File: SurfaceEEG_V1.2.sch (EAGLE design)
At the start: 52 parts

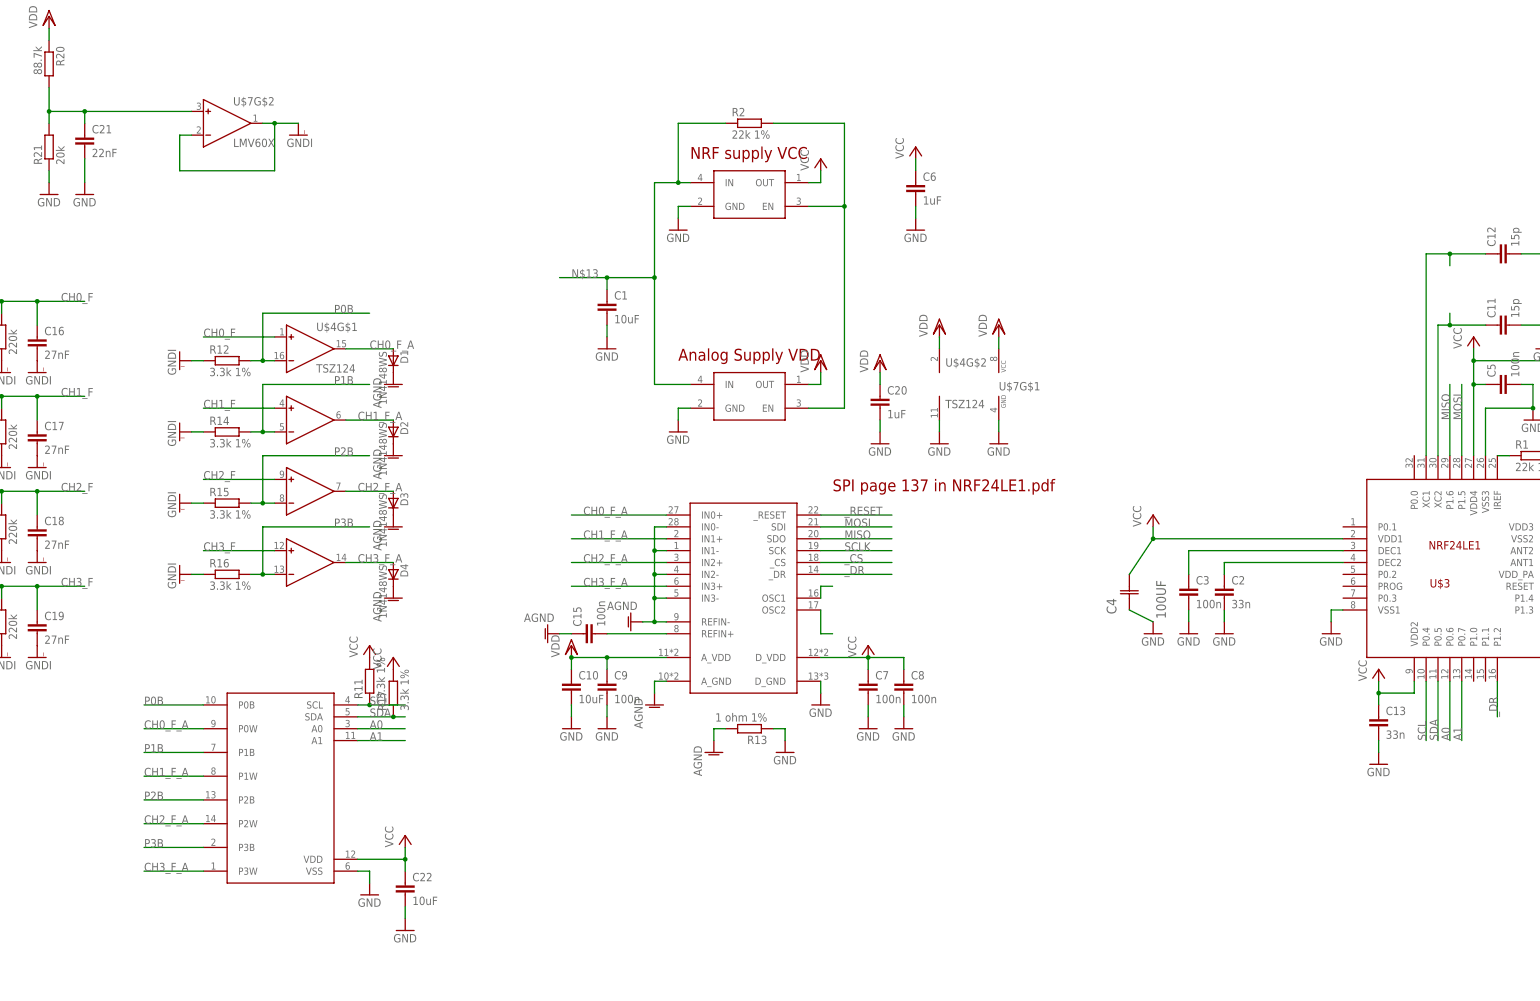
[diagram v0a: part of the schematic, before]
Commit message: Replaced components with ones from our libraries
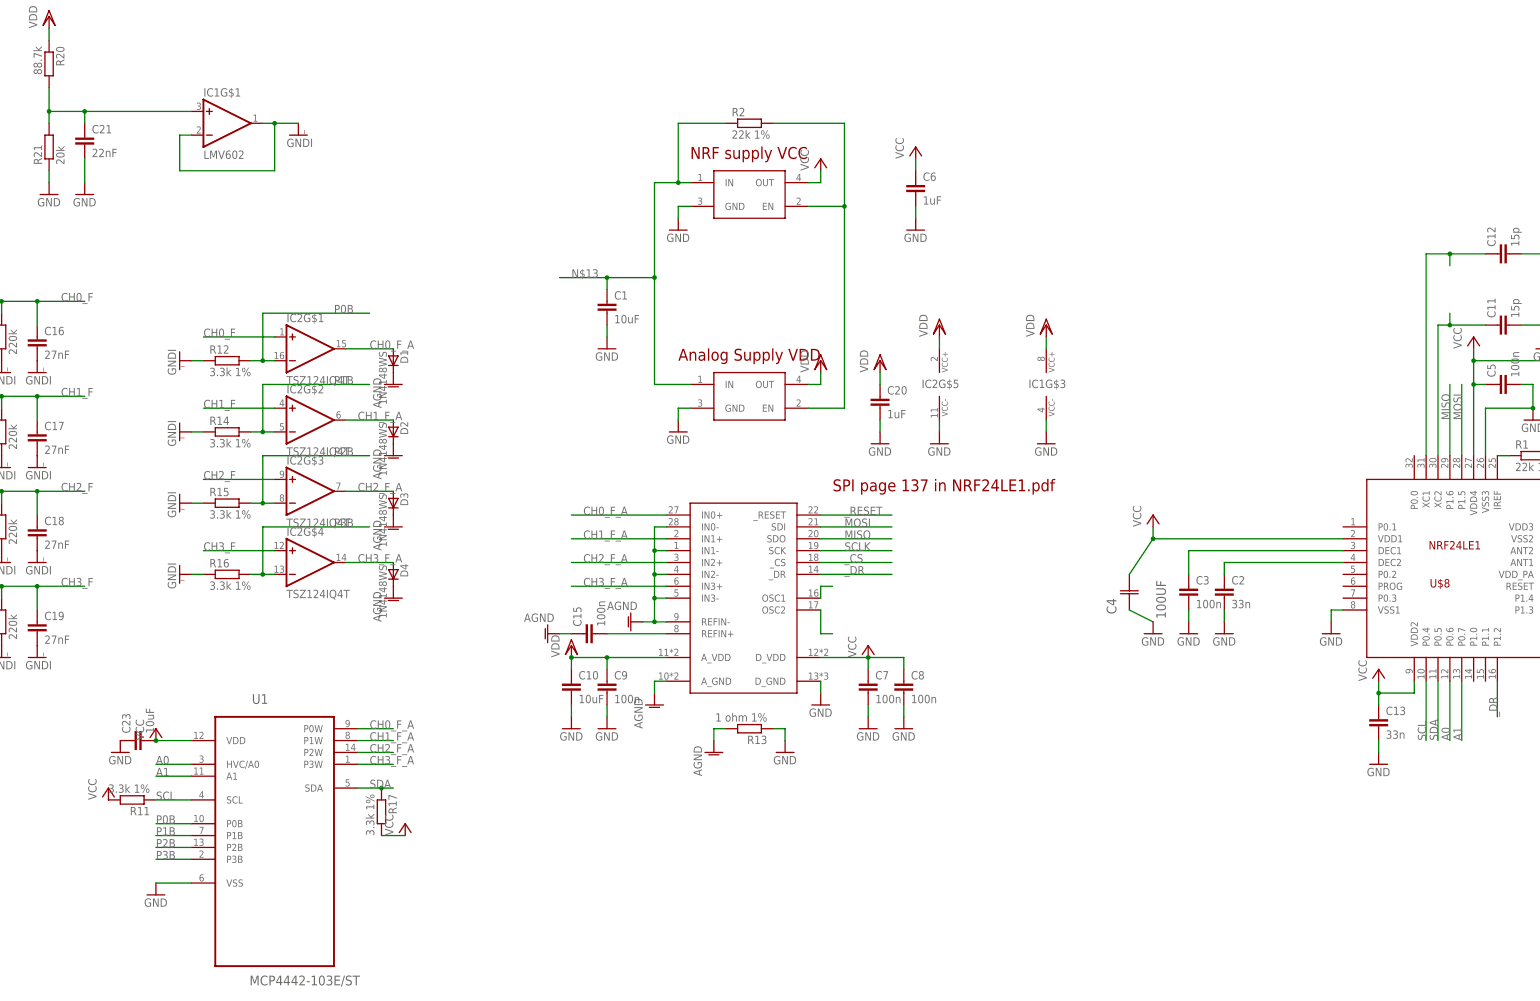
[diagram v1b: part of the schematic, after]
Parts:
- removed C22: 10uF, ELL-i-Passives:C0603
- removed U$4: TSZ124, st-microelectronics:TSZ124
- removed U$5: NCP103, on-semiconductor:NCP103
- removed U$6: MCP444X, microchip:MCP444X
- removed U$7: LMV60X, texas:LMV60X
- added C23: 10uF, ELL-i-Passives:C0603
- added IC1: LMV602, (custom)-new-components:LMV602
- added IC2: TSZ124IQ4T, (user-cadsoft)-st-microelectronics-tsz12x:TSZ124IQ4T
- added U$8: NRF24LE1, (misc)-parts-that-we-use:NRF24LE1
- added U1: MCP4442-103E/ST, (manufact)-Microchip-MCP44-farnell:MCP4442-103E/ST
- U$1: value MCP3912 -> NCP103; device microchip:MCP3912 -> (custom)-new-components:NCP103
- U$2: device on-semiconductor:NCP103 -> (custom)-new-components:NCP103
- U$3: value NRF24LE1 -> MCP3912; device SparkFun-RF:NRF24LE1 -> (custom)-new-components:MCP3912
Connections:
- net A0: now also U$8.P0.6, U1.HVC/A0; no longer U$3.P0.6, U$6.A0
- net A1: now also U$8.P0.7, U1.A1; no longer U$3.P0.7, U$6.A1
- net AGND: now also U$3.A_GND, U$3.IN0-, U$3.IN1-, U$3.IN2-, U$3.IN3-, U$3.REFIN-; no longer U$1.A_GND, U$1.IN0-, U$1.IN1-, U$1.IN2-, U$1.IN3-, U$1.REFIN-
- net CH0_F: now also IC2G$1.IN+; no longer U$4G$1.IN+
- net CH0_F_A: now also IC2G$1.OUT, U$3.IN0+, U1.P0W; no longer U$1.IN0+, U$4G$1.OUT, U$6.P0W
- net CH1_F: now also IC2G$2.IN+; no longer U$4G$1.IN+1
- net CH1_F_A: now also IC2G$2.OUT, U$3.IN1+, U1.P1W; no longer U$1.IN1+, U$4G$1.OUT1, U$6.P1W
- net CH2_F: now also IC2G$3.IN+; no longer U$4G$1.IN+2
- net CH2_F_A: now also IC2G$3.OUT, U$3.IN2+, U1.P2W; no longer U$1.IN2+, U$4G$1.OUT2, U$6.P2W
- net CH3_F: now also IC2G$4.IN+; no longer U$4G$1.IN+3
- net CH3_F_A: now also IC2G$4.OUT, U$3.IN3+, U1.P3W; no longer U$1.IN3+, U$4G$1.OUT3, U$6.P3W
- net GND: now also C23.1, IC1G$3.VCC-, IC2G$5.VCC-, U$1.GND, U$3.D_GND, U$8.VSS1, U$8.VSS2, U$8.VSS3, U1.VSS; no longer C22.2, U$1.D_GND, U$3.VSS1, U$3.VSS2, U$3.VSS3, U$4G$2.V-, U$5.GND, U$6.VSS, U$7G$1.GND
- net GNDI: now also IC1G$1.IN-, IC1G$1.OUT; no longer U$7G$2.IN-, U$7G$2.OUT
- net MISO: now also U$3.SDO, U$8.P1.6; no longer U$1.SDO, U$3.P1.6
- net MOSI: now also U$3.SDI, U$8.P1.5; no longer U$1.SDI, U$3.P1.5
- net N$10: now also U$8.XC2; no longer U$3.XC2
- net N$11: now also U$8.XC1; no longer U$3.XC1
- net N$12: now also U$3.REFIN+; no longer U$1.REFIN+
- net N$13: now also U$1.IN; no longer U$5.IN
- net N$14: now also U$3.OSC1; no longer U$1.OSC1
- net N$15: now also U$3.OSC2; no longer U$1.OSC2
- net N$18: now also IC1G$1.IN+; no longer U$7G$2.IN+
- net N$2: now also U$8.DEC1; no longer U$3.DEC1
- net N$3: now also U$8.DEC2; no longer U$3.DEC2
- net N$5: now also U$1.EN; no longer U$5.EN
- net N$6: now also U$8.ANT2; no longer U$3.ANT2
- net N$7: now also U$8.ANT1; no longer U$3.ANT1
- net N$8: now also U$8.VDD_PA; no longer U$3.VDD_PA
- net N$9: now also U$8.IREF; no longer U$3.IREF
- net P0B: now also IC2G$1.IN-, U1.P0B; no longer U$4G$1.IN-, U$6.P0B
- net P1B: now also IC2G$2.IN-, U1.P1B; no longer U$4G$1.IN-1, U$6.P1B
- net P2B: now also IC2G$3.IN-, U1.P2B; no longer U$4G$1.IN-2, U$6.P2B
- net P3B: now also IC2G$4.IN-, U1.P3B; no longer U$4G$1.IN-3, U$6.P3B
- net SCL: now also U$8.P0.4, U1.SCL; no longer U$3.P0.4, U$6.SCL
- net SCLK: now also U$3.SCK, U$8.P1.4; no longer U$1.SCK, U$3.P1.4
- net SDA: now also U$8.P0.5, U1.SDA; no longer U$3.P0.5, U$6.SDA
- net VCC: now also C23.2, U$1.OUT, U$3.D_VDD, U$8.VDD1, U$8.VDD2, U$8.VDD3, U$8.VDD4, U1.VDD; no longer C22.1, U$1.D_VDD, U$2.OUT, U$3.VDD1, U$3.VDD2, U$3.VDD3, U$3.VDD4, U$6.VDD
- net VDD: now also IC1G$3.VCC+, IC2G$5.VCC+, U$2.OUT, U$3.A_VDD; no longer U$1.A_VDD, U$4G$2.V+, U$5.OUT, U$7G$1.VCC
- net _CS: now also U$3._CS, U$8.P1.3; no longer U$1._CS, U$3.P1.3
- net _DR: now also U$3._DR, U$8.P1.2; no longer U$1._DR, U$3.P1.2
- net _RESET: now also U$3._RESET; no longer U$1._RESET
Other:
- moved on the sheet: R11, R17

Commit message: Added RF antenna schematics
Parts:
- removed C5: 100n, ELL-i-Passives:C0402
- added ANTENNA_CHIP: (no value), ELL-i-Passives:R0805
- added C22: 2.2nF, ELL-i-Passives:C0603
- added C24: 0.1uF, (manufact)-capacitors-AVX-element14:04023C104KAT2A
- added C25: 1pF, (manufact)-capacitors-AVX-element14:UQCL2A1R0BAT2A/500
- added C26: 4.7pF, (manufact)-capacitors-AVX-element14:UQCL2A4R7CAT2A/500
- added FB1, FB2: 6.8nH, ELL-i-Passives:FB0402
- added FB3: 4.7nH, ELL-i-Passives:FB0402
- C14: value 2.2n -> 1.5pF; device ELL-i-Passives:C0402 -> (manufact)-capacitors-AVX-element14:UQCL2A1R5BAT2A/500
- C3: value 100n -> 0.1uF; device ELL-i-Passives:C0402 -> (manufact)-capacitors-AVX-element14:04023C104KAT2A
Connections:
- removed net N$6: U$8.ANT2
- removed net N$8: C14.1, U$8.VDD_PA
- new net ANT: ANTENNA_CHIP.1, C14.C2, C25.C2
- new net N$1: FB2.1, FB3.1, U$8.ANT2
- new net N$22: C14.C1, FB3.2
- new net N$4: C22.1, C26.C2, FB1.1, U$8.VDD_PA
- net GND: now also C22.2, C24.C1, C25.C1, C26.C1, C3.C1; no longer C14.2, C3.2, C5.2
- net N$2: now also C24.C2; no longer C3.1
- net N$7: now also FB1.2, FB2.2
- net VCC: now also C3.C2; no longer C5.1

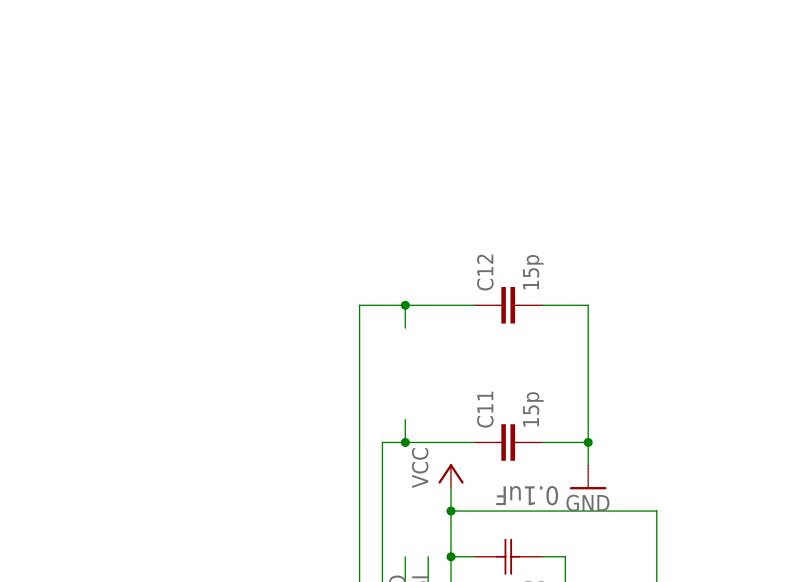
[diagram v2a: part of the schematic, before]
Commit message: Add crystal 16 MHz
Add crystal 16 MHz for NRF24LE1
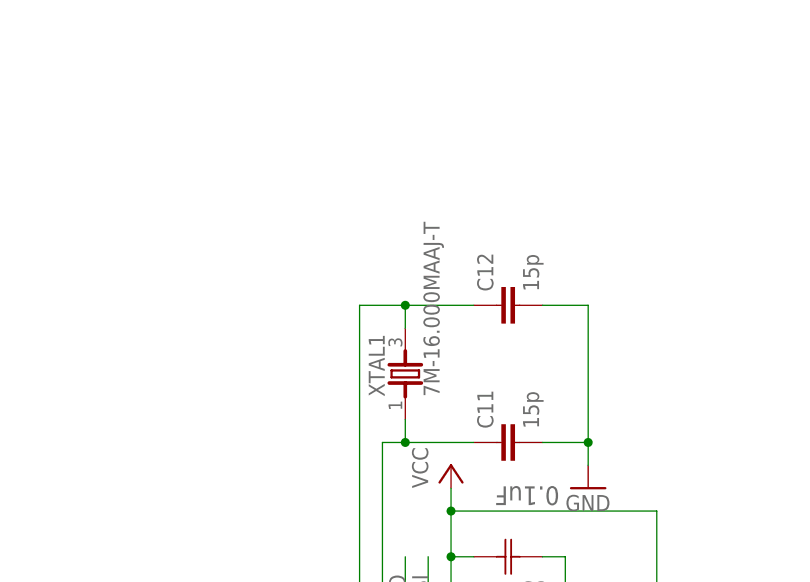
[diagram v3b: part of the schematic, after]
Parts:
- added XTAL1: 7M-16.000MAAJ-T, (misc)-parts-that-we-use:7M-16.000MAAJ-T
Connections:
- net N$10: now also XTAL1.1
- net N$11: now also XTAL1.3
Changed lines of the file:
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@@
 <part name="C24" library="(manufact)-capacitors-AVX-element14" deviceset="04023C104KAT2A" device="" value="0.1uF"/>
 <part name="C3" library="(manufact)-capacitors-AVX-element14" deviceset="04023C104KAT2A" device="" value="0.1uF"/>
+<part name="XTAL1" library="(misc)-parts-that-we-use" deviceset="7M-16.000MAAJ-T" device=""/>
 </parts>
 <sheets>
@@
 <instance part="C24" gate="A" x="149.86" y="93.98" rot="R90"/>
 <instance part="C3" gate="A" x="220.98" y="142.24" rot="R180"/>
+<instance part="XTAL1" gate="A" x="205.74" y="162.56" rot="R90"/>
 </instances>
 <busses>
@@
 <junction x="205.74" y="154.94"/>
 <pinref part="U$8" gate="G$1" pin="XC2"/>
+<pinref part="XTAL1" gate="A" pin="1"/>
 </segment>
 </net>
@@
 <junction x="205.74" y="170.18"/>
 <pinref part="U$8" gate="G$1" pin="XC1"/>
-</segment>
-</net>
+<pinref part="XTAL1" gate="A" pin="3"/>
+</segment>
+</net>

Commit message: Created almost finished board, fixed schematics
Schematics was switched for 3 differential + 1 relative to ground measurements, board was designed accordingly
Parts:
- removed C22: 2.2nF, ELL-i-Passives:C0603
- removed C26: 4.7pF, (manufact)-capacitors-AVX-element14:UQCL2A4R7CAT2A/500
- removed R13: 1 ohm 1%, ELL-i-Passives:R0603
- removed R21: 20k, ELL-i-Passives:R0603
- added C27: 10uF, (manufact)-Kemet-element14:C0603C106M9PACTU
- added C28: 0.1uF, (manufact)-Kemet-element14:C0603C104K5RAC-TU
- added C5: 15pF, (manufact)-capacitors-AVX-element14:UQCL2A150JAT2A/500
- added JP1, JP2, JP3, JP4, JP5, JP6, JP7, JP8: (no value), adafruit:PINHD-1X1
- added R18: 3.3K Ohms, (manufact)-resistors-YAGEO-element14:RC0603FR-073K3L
- added R19: 88.7K EDIT, (manufact)-resistors-YAGEO-element14:RT0603FRE0782KL
- added XTAL2: 7M-16.000MAAJ-T, (misc)-parts-that-we-use:7M-16.000MAAJ-T
- C1: value 10uF -> 0.1uF; device ELL-i-Passives:C0603 -> (manufact)-Kemet-element14:C0603C104K5RAC-TU
- C10, C23: device ELL-i-Passives:C0603 -> (manufact)-Kemet-element14:C0603C106M9PACTU
- C11, C12: value 15p -> 15pF; device ELL-i-Passives:C0402 -> (manufact)-capacitors-AVX-element14:UQCL2A150JAT2A/500
- C13: value 33n -> 47nF; device ELL-i-Passives:C0402 -> (manufact)-Kemet-element14:C0603C473K1RACTU
- C15: value 100n -> 47nF; device ELL-i-Passives:C0402 -> (manufact)-Kemet-element14:C0603C473K1RACTU
- C16, C17, C18: value 27nF -> 0.027UF; device ELL-i-Passives:C0603 -> (manufact)-capacitors-AVX-element14:0603YC273JAT2A
- C19: value 27nF -> 15pF; device ELL-i-Passives:C0603 -> (manufact)-capacitors-AVX-element14:UQCL2A150JAT2A/500
- C2: value 33n -> 100nF; device ELL-i-Passives:C0402 -> (manufact)-capacitors-AVX-element14:06033C104JAT2A
- C20: value 1uF -> 0.027UF; device ELL-i-Passives:C0402 -> (manufact)-capacitors-AVX-element14:0603YC273JAT2A
- C21: value 22nF -> 47nF; device ELL-i-Passives:C0603 -> (manufact)-Kemet-element14:C0603C473K1RACTU
- C6: value 1uF -> 2.2nF; device ELL-i-Passives:C0402 -> (manufact)-Kemet-element14:C0402C222K5RACTU
- C7, C8, C9: value 100n -> 100nF; device ELL-i-Passives:C0402 -> (manufact)-capacitors-AVX-element14:06033C104JAT2A
- R1: value 22k 1% -> 22K Ohms; device ELL-i-Passives:R0603 -> (manufact)-resistors-YAGEO-element14:RC0603FR-0722KL
- R10, R11, R12, R14, R15, R16, R4, R6, R8: value 3.3k 1% -> 3.3K Ohms; device ELL-i-Passives:R0603 -> (manufact)-resistors-YAGEO-element14:RC0603FR-073K3L
- R17: value 3.3k 1% -> 220K Ohms; device ELL-i-Passives:R0603 -> (manufact)-resistors-YAGEO-element14:RC0603FR-07220KL
- R2: value 22k 1% -> 20K Ohms; device ELL-i-Passives:R0603 -> (manufact)-resistors-YAGEO-element14:RC0603FR-0720KL
- R20: value 88.7k -> 0 Ohm; device ELL-i-Passives:R0603 -> (manufact)-resistors-YAGEO-element14:9C06031A0R00JLHFT
- R3, R5, R7: value 220k -> 220K Ohms; device ELL-i-Passives:R0603 -> (manufact)-resistors-YAGEO-element14:RC0603FR-07220KL
- R9: value 220k -> 22K Ohms; device ELL-i-Passives:R0603 -> (manufact)-resistors-YAGEO-element14:RC0603FR-0722KL
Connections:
- removed net N$13: C1.1, R2.1, U$1.IN, U$2.IN
- removed net N$9: R1.1, U$8.IREF
- new net N$6: R9.R2, U$8.IREF
- new net VIN: C10.C2, JP5.1, R1.R2, U$1.IN, U$2.IN
- net AGND: now also C9.C2, R20.R2; no longer C15.1, D1.C, D2.C, D3.C, D4.C, R13.2, U$3.IN0-, U$3.IN1-, U$3.IN2-, U$3.IN3-, U$3.REFIN-
- net CH0: now also JP1.1, R18.R2; no longer R4.2
- net CH0_F: now also C20.C2, R17.R1, R18.R1; no longer C16.1, R3.2, R4.1
- net CH0_F_A: now also U$3.IN1+, U$3.IN2+, U$3.IN3+
- net CH1: now also JP2.1, R4.R2; no longer R6.2
- net CH1_F: now also C16.C2, R3.R1, R4.R1; no longer C17.1, R5.2, R6.1
- net CH1_F_A: now also U$3.IN0-; no longer U$3.IN1+
- net CH2: now also JP3.1, R6.R2; no longer R8.2
- net CH2_F: now also C17.C2, R5.R1, R6.R1; no longer C18.1, R7.2, R8.1
- net CH2_F_A: now also U$3.IN1-; no longer U$3.IN2+
- net CH3: now also JP4.1, R8.R2; no longer R10.2
- net CH3_F: now also C18.C2, R7.R1, R8.R1; no longer C19.1, R10.1, R9.2
- net CH3_F_A: now also U$3.IN2-; no longer U$3.IN3+
- net GND: now also C1.C1, C10.C1, C11.C2, C12.C2, C13.C1, C15.C1, C19.C2, C2.C1, C21.C1, C23.C1, C27.C1, C28.C1, C5.C2, C6.C1, C7.C1, C8.C1, JP6.1, JP8.1, R2.R2, R20.R1; no longer C1.2, C10.2, C11.2, C12.2, C13.2, C2.2, C20.2, C21.2, C22.2, C23.1, C26.C1, C6.2, C7.2, C8.2, C9.2, R13.1, R21.1
- net GNDI: now also C16.C1, C17.C1, C18.C1, C20.C1, D1.C, D2.C, D3.C, D4.C, JP7.1, R10.R2, R12.R2, R14.R2, R15.R2, R17.R2, R3.R2, R5.R2, R7.R2, U$3.IN3-, U$3.REFIN-; no longer C16.2, C17.2, C18.2, C19.2, R12.1, R14.1, R15.1, R16.1, R3.1, R5.1, R7.1, R9.1
- net N$10: now also C5.C1; no longer C11.1
- net N$11: now also C19.C1; no longer C12.1
- net N$12: now also C9.C1; no longer C15.2
- net N$14: now also C11.C1, XTAL2.3
- net N$15: now also C12.C1, XTAL2.1
- net N$18: now also C15.C2, R19.R2, R2.R1; no longer C21.1, R20.2, R21.2
- net N$3: now also C21.C2; no longer C2.1
- net N$4: now also C6.C2; no longer C22.1, C26.C2
- net N$5: now also R1.R1; no longer R2.2
- net P0B: now also R10.R1; no longer R12.2
- net P1B: now also R12.R1; no longer R14.2
- net P2B: now also R14.R1; no longer R15.2
- net P3B: now also R15.R1; no longer R16.2
- net SCL: now also R16.R1; no longer R11.1
- net SDA: now also R11.R2; no longer R17.1
- net VCC: now also C13.C2, C2.C2, C27.C2, C28.C2, C7.C2, R11.R1, R16.R2, R9.R1; no longer C13.1, C23.2, C6.1, C7.1, C8.1, R1.2, R11.2, R17.2
- net VDD: now also C1.C2, C23.C2, C8.C2, R19.R1; no longer C10.1, C20.1, C9.1, R20.1
